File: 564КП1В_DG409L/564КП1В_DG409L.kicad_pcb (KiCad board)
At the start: 2 copper layers, 12 x 12 mm, 4 parts

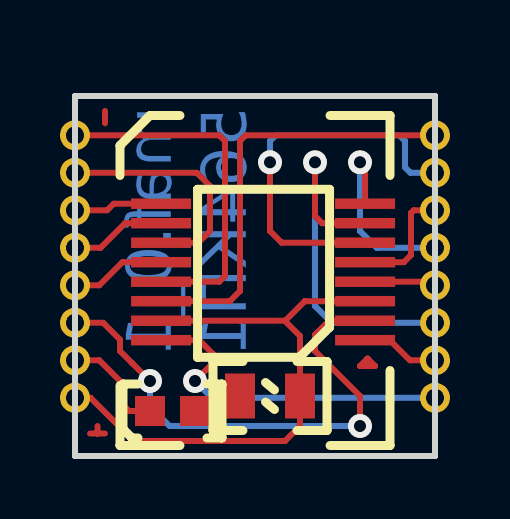
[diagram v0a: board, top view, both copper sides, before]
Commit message: увеличены зазоры и квадратизированы площадки
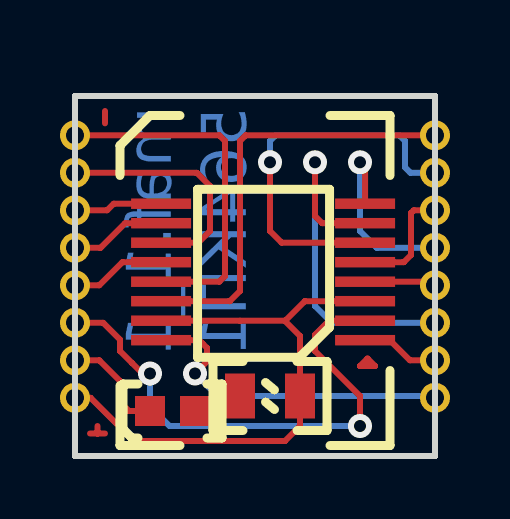
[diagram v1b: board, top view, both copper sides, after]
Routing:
- net B: track 11.3 -> 10.6 mm
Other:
- board text added: "maf.1_1"
- board text removed: "maf.0_1"
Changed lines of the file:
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@@
     (thickness 1.6)
     (drawings 6)
-    (tracks 112)
+    (tracks 113)
     (zones 0)
     (modules 4)
@@
     (mod_text_size 1 1)
     (mod_text_width 0.15)
-    (pad_size 1.524 1.524)
-    (pad_drill 0.762)
+    (pad_size 1 1)
+    (pad_drill 0.6)
     (pad_to_mask_clearance 0.05)
     (solder_mask_min_width 0.2)
@@
       (drillshape 0)
       (scaleselection 1)
-      (outputdirectory "maf_1/"))
+      (outputdirectory "maf1_1/"))
   )
   (net 0 "")
@@
   (gr_line (start 137 100) (end 149 100) (layer Edge.Cuts) (width 0.2))
   (gr_line (start 137 88) (end 137 100) (layer Edge.Cuts) (width 0.2))
-  (gr_text maf.0_1 (at 139.5 92.5 90) (layer B.Cu)
+  (gr_text maf.1_1 (at 139.5 92.5 90) (layer B.Cu)
     (effects (font (size 1.5 1.5) (thickness 0.3)) (justify mirror))
   )
@@
   (segment (start 146.67 94.19) (end 148.879999 94.19) (width 0.2) (layer F.Cu) (net 10))
   (segment (start 137 95.560001) (end 137.939999 95.560001) (width 0.2) (layer F.Cu) (net 11))
-  (via (at 139.5 97.5) (size 0.8) (drill 0.4) (layers F.Cu B.Cu) (net 11))
+  (via (at 139.5 97.25) (size 0.8) (drill 0.4) (layers F.Cu B.Cu) (net 11))
   (segment (start 137.939999 95.560001) (end 138.5 96.120002) (width 0.2) (layer F.Cu) (net 11))
   (via (at 146.5 99) (size 0.8) (drill 0.4) (layers F.Cu B.Cu) (net 11))
@@
   (segment (start 140 99.5) (end 138.959998 99.5) (width 0.2) (layer F.Cu) (net 15))
   (segment (start 140 99.5) (end 144 99.5) (width 0.2) (layer F.Cu) (net 15))
-  (via (at 141 97.5) (size 0.8) (drill 0.4) (layers F.Cu B.Cu) (net 16))
-  (segment (start 141.560001 98.060001) (end 141 97.5) (width 0.2) (layer B.Cu) (net 16))
-  (segment (start 149 98.060001) (end 141.560001 98.060001) (width 0.2) (layer B.Cu) (net 16))
-  (segment (start 141.599999 96.900001) (end 141 97.5) (width 0.2) (layer F.Cu) (net 16))
-  (segment (start 141.599999 96.599999) (end 141.599999 96.900001) (width 0.2) (layer F.Cu) (net 16))
-  (segment (start 141.14 96.14) (end 141.599999 96.599999) (width 0.2) (layer F.Cu) (net 16))
   (segment (start 139.87 96.14) (end 141.14 96.14) (width 0.2) (layer F.Cu) (net 16))
+  (segment (start 141.399999 96.399999) (end 141.25 96.25) (width 0.2) (layer F.Cu) (net 16))
+  (segment (start 141.399999 96.850001) (end 141.399999 96.399999) (width 0.2) (layer F.Cu) (net 16))
+  (segment (start 141 97.25) (end 141.399999 96.850001) (width 0.2) (layer F.Cu) (net 16))
+  (segment (start 141.14 96.14) (end 141.25 96.25) (width 0.2) (layer F.Cu) (net 16))
+  (via (at 141 97.25) (size 0.8) (drill 0.4) (layers F.Cu B.Cu) (net 16))
+  (segment (start 141.75 98) (end 148.59999 98) (width 0.2) (layer B.Cu) (net 16))
+  (segment (start 141 97.25) (end 141.75 98) (width 0.2) (layer B.Cu) (net 16))
   (segment (start 141.8 98) (end 142.5 98) (width 0.2) (layer F.Cu) (net 17))
   (segment (start 141.8 98.4) (end 141.8 98) (width 0.2) (layer F.Cu) (net 17))
